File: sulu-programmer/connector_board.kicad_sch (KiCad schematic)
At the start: 12 parts, among them J1 Conn_01x08, J2 Conn_02x04_Top_Bottom

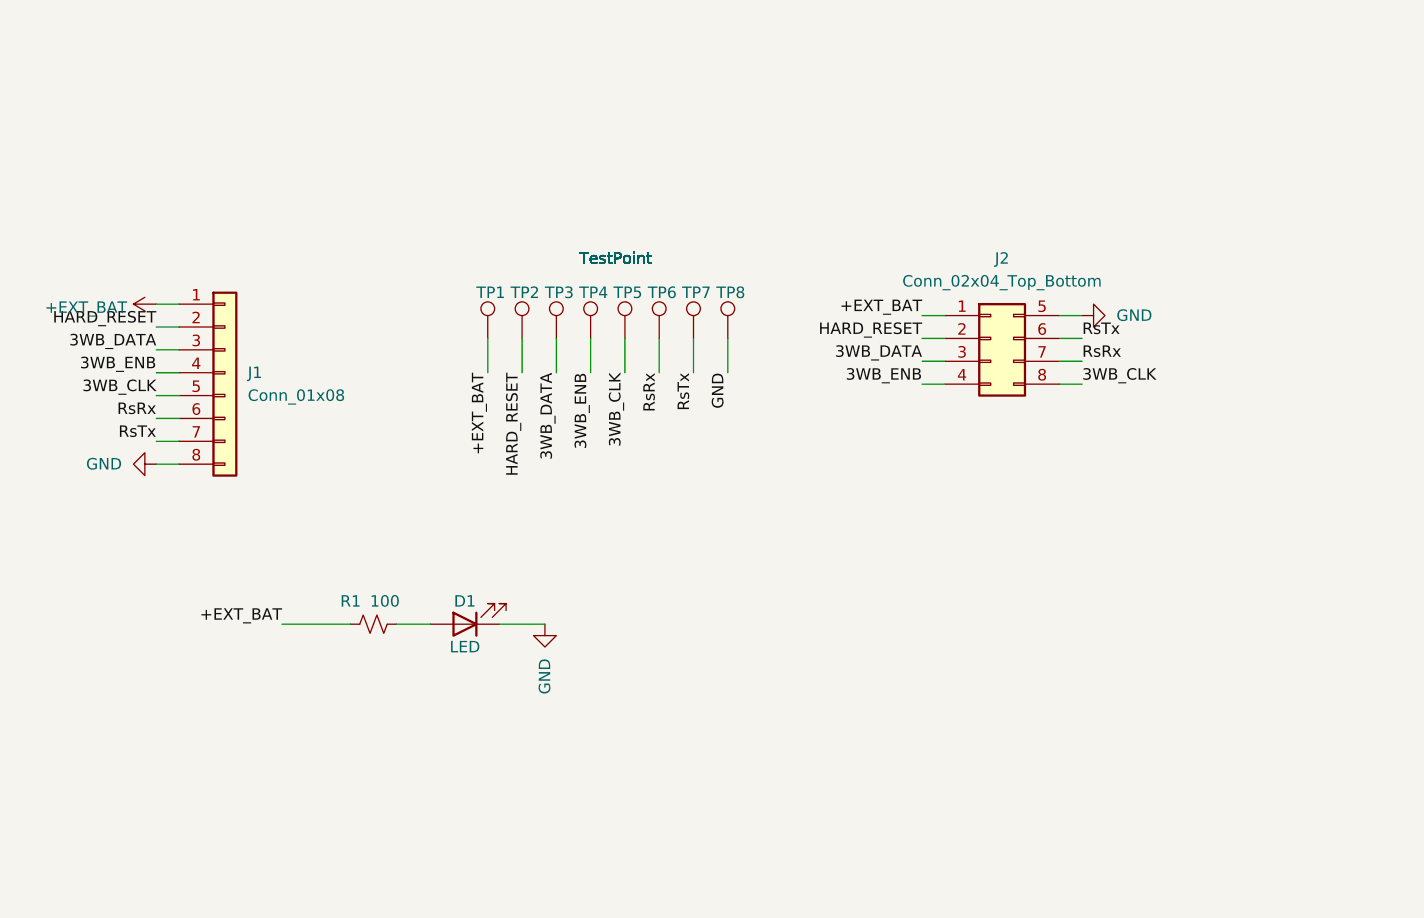
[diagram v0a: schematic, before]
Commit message: Updated connector boards and Sulu-ADS1299 schematic
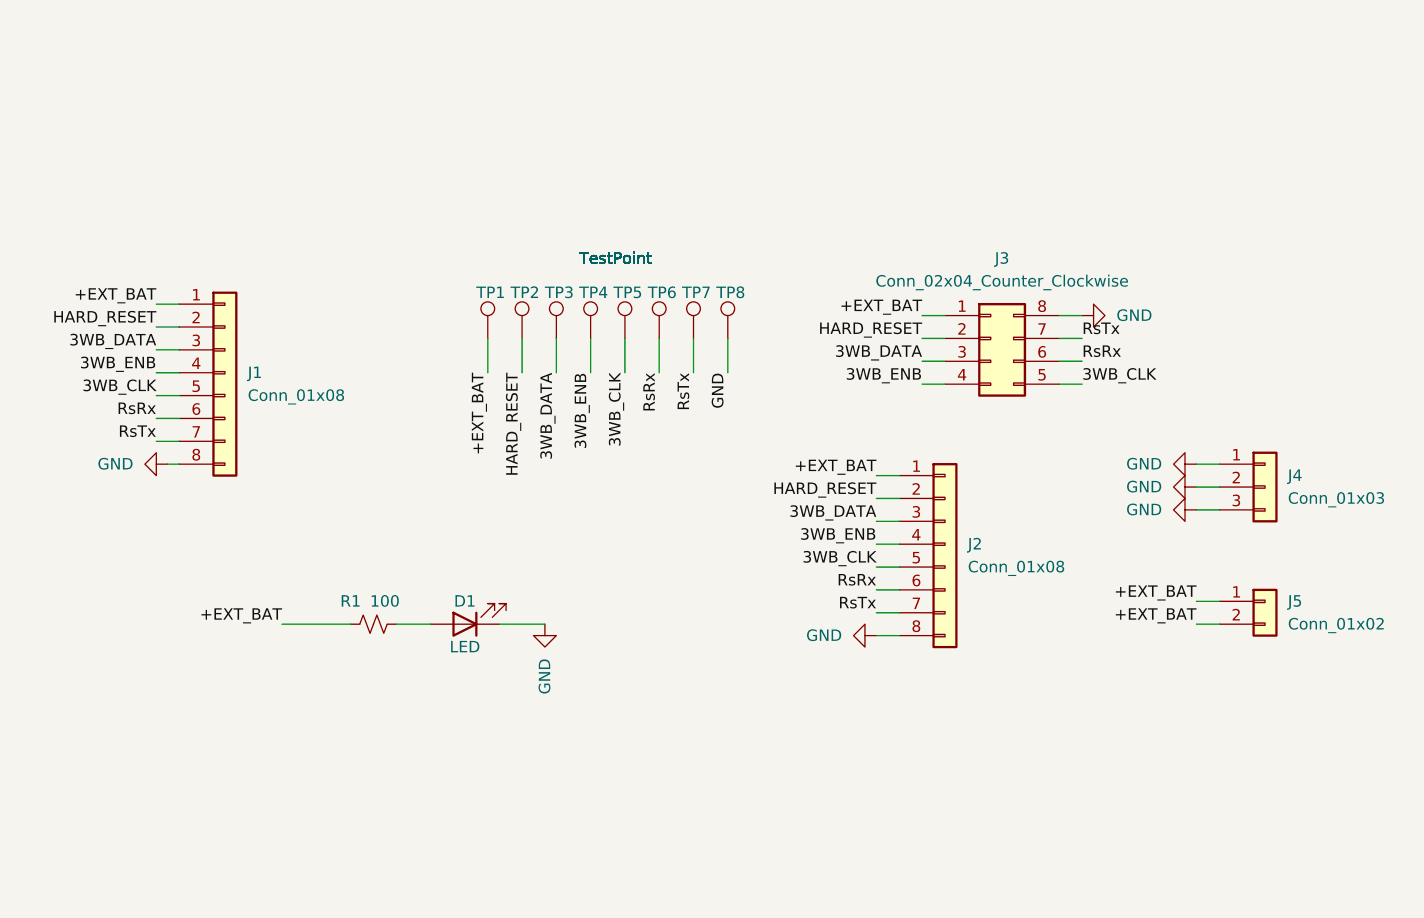
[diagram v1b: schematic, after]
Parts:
- removed J2: Conn_02x04_Top_Bottom, Connector_PinHeader_2.54mm:PinHeader_2x04_P2.54mm_Vertical, symbol Connector_Generic:Conn_02x04_Top_Bottom
- added J2: Conn_01x08, Connector_PinHeader_2.54mm:PinHeader_1x08_P2.54mm_Vertical, symbol Connector_Generic:Conn_01x08
- added J3: Conn_02x04_Counter_Clockwise, Connector_PinHeader_2.54mm:PinHeader_2x04_P2.54mm_Vertical, symbol Connector_Generic:Conn_02x04_Counter_Clockwise
- added J4: Conn_01x03, Connector_PinHeader_2.54mm:PinHeader_1x03_P2.54mm_Vertical, symbol Connector_Generic:Conn_01x03
- added J5: Conn_01x02, Connector_PinHeader_2.54mm:PinHeader_1x02_P2.54mm_Vertical, symbol Connector_Generic:Conn_01x02
- TP1, TP2, TP3, TP4, TP5, TP6, TP7, TP8: footprint SCUM:through_hole -> TestPoint:TestPoint_Plated_Hole_D2.0mm
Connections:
- net +EXT_BAT: now also J2.1 (Pin_1), J3.1 (Pin_1), J5.1 (Pin_1), J5.2 (Pin_2)
- net 3WB_CLK: now also J2.5 (Pin_5), J3.5 (Pin_5)
- net 3WB_DATA: now also J2.3 (Pin_3), J3.3 (Pin_3)
- net 3WB_ENB: now also J2.4 (Pin_4), J3.4 (Pin_4)
- net GND: now also J2.8 (Pin_8), J3.8 (Pin_8), J4.1 (Pin_1), J4.2 (Pin_2), J4.3 (Pin_3)
- net HARD_RESET: now also J2.2 (Pin_2), J3.2 (Pin_2)
- net RsRx: now also J2.6 (Pin_6), J3.6 (Pin_6)
- net RsTx: now also J2.7 (Pin_7), J3.7 (Pin_7)

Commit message: Sulu-ADS1299 and connector board layout+sch progress
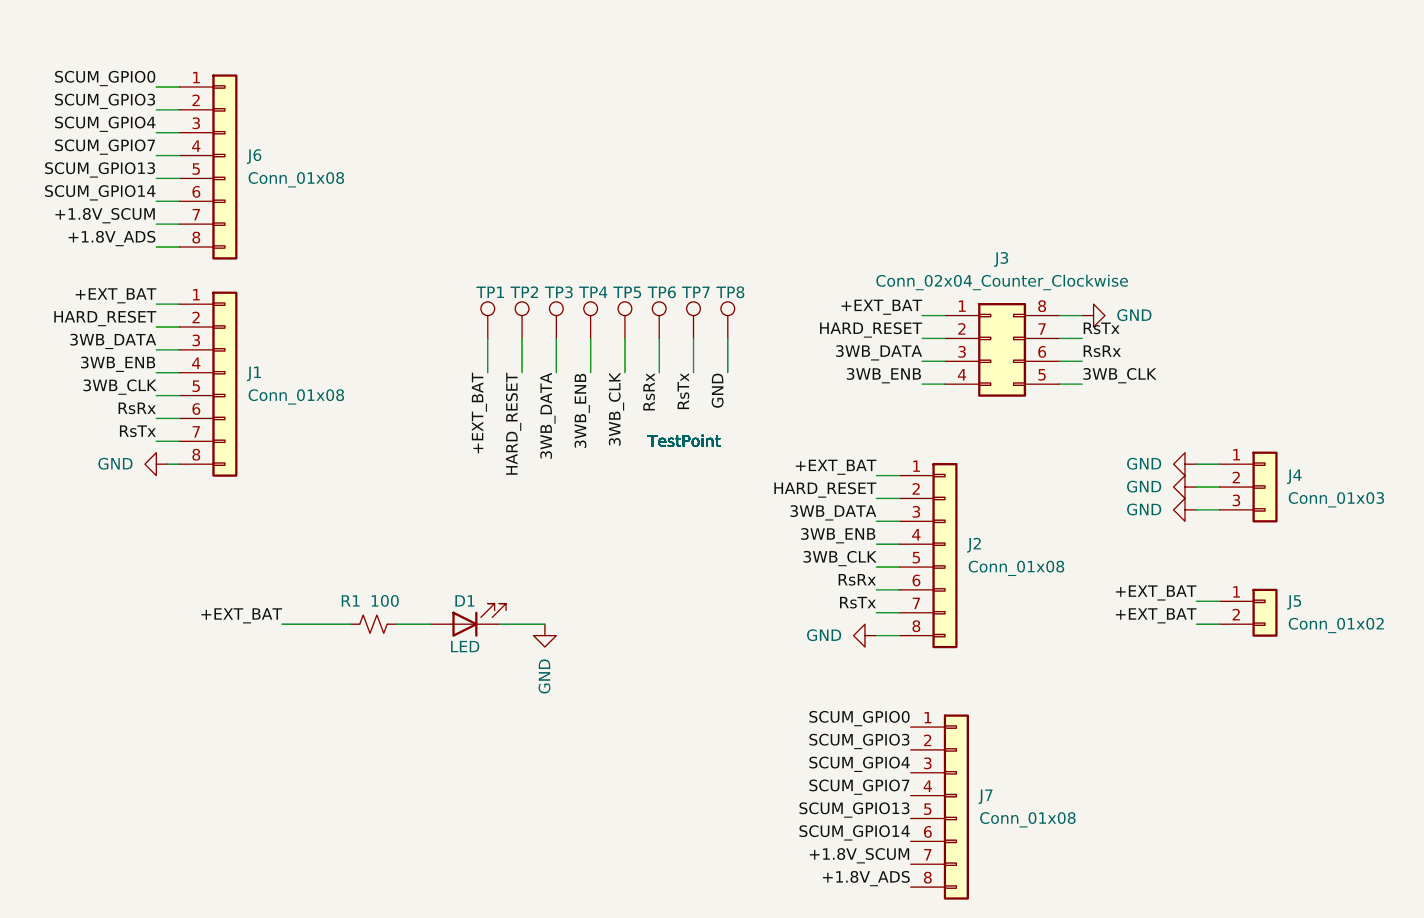
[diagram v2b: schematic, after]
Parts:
- added J6: Conn_01x08, Connector_Molex:Molex_PicoBlade_53047-0810_1x08_P1.25mm_Vertical, symbol Connector_Generic:Conn_01x08
- added J7: Conn_01x08, Connector_PinHeader_2.54mm:PinHeader_1x08_P2.54mm_Vertical, symbol Connector_Generic:Conn_01x08
- TP1, TP2, TP3, TP4, TP5, TP6, TP7, TP8: footprint TestPoint:TestPoint_Plated_Hole_D2.0mm -> TestPoint:TestPoint_THTPad_1.0x1.0mm_Drill0.5mm
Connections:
- new net +1.8V_ADS: J6.8 (Pin_8), J7.8 (Pin_8)
- new net +1.8V_SCUM: J6.7 (Pin_7), J7.7 (Pin_7)
- new net SCUM_GPIO0: J6.1 (Pin_1), J7.1 (Pin_1)
- new net SCUM_GPIO13: J6.5 (Pin_5), J7.5 (Pin_5)
- new net SCUM_GPIO14: J6.6 (Pin_6), J7.6 (Pin_6)
- new net SCUM_GPIO3: J6.2 (Pin_2), J7.2 (Pin_2)
- new net SCUM_GPIO4: J6.3 (Pin_3), J7.3 (Pin_3)
- new net SCUM_GPIO7: J6.4 (Pin_4), J7.4 (Pin_4)

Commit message: SCuM Programmer Rev. 2, submitted for fab
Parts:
- added TP10, TP11, TP12, TP9: TestPoint, TestPoint:TestPoint_Keystone_5010-5014_Multipurpose, symbol Connector:TestPoint
- R1: value 100 -> 300
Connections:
- net GND: now also TP10.1, TP11.1, TP12.1, TP9.1
